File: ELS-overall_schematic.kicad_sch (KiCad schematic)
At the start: 3 parts, among them J1 DE9_Plug, J2 DE9_Plug, U1 LTC2851HDD

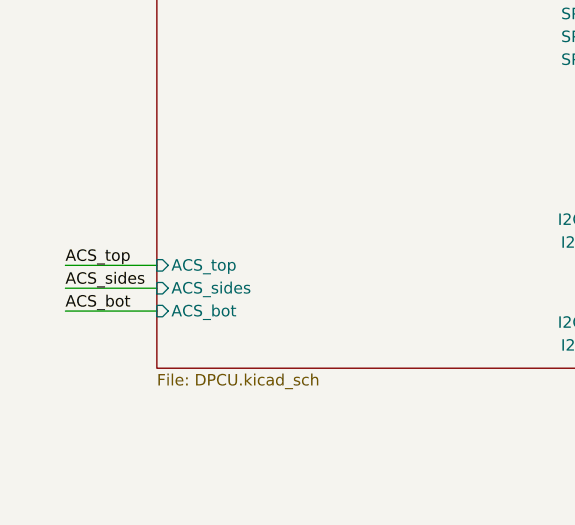
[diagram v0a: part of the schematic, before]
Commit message: Add voltage divider for adj signals
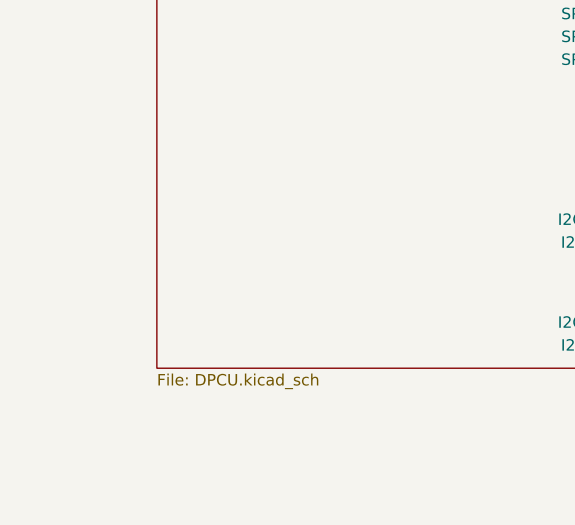
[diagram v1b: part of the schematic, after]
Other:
- sheet DPCU ports: added none; removed ACS_bot, ACS_sides, ACS_top
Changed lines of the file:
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@@
 	(wire
 		(pts
-			(xy 33.02 161.29) (xy 22.86 161.29)
-		)
-		(stroke
-			(width 0)
-			(type default)
-		)
-	)
-	(wire
-		(pts
 			(xy 153.67 77.47) (xy 163.83 77.47)
 		)
@@
 	(wire
 		(pts
-			(xy 33.02 163.83) (xy 22.86 163.83)
-		)
-		(stroke
-			(width 0)
-			(type default)
-		)
-	)
-	(wire
-		(pts
 			(xy 153.67 176.53) (xy 163.83 176.53)
 		)
@@
 	(wire
 		(pts
-			(xy 33.02 158.75) (xy 22.86 158.75)
-		)
-		(stroke
-			(width 0)
-			(type default)
-		)
-	)
-	(wire
-		(pts
 			(xy 203.2 118.11) (xy 195.58 118.11)
 		)
@@
 		)
 	)
-	(label "ACS_bot"
-		(at 22.86 163.83 0)
-		(fields_autoplaced yes)
-		(effects
-			(font
-				(size 1.27 1.27)
-			)
-			(justify left bottom)
-		)
-	)
 	(label "SDA2"
 		(at 203.2 83.82 180)
@@
 		)
 	)
-	(label "ACS_top"
-		(at 22.86 158.75 0)
-		(fields_autoplaced yes)
-		(effects
-			(font
-				(size 1.27 1.27)
-			)
-			(justify left bottom)
-		)
-	)
 	(label "SDA2"
 		(at 203.2 19.05 180)
@@
 		)
 	)
-	(label "ACS_sides"
-		(at 22.86 161.29 0)
-		(fields_autoplaced yes)
-		(effects
-			(font
-				(size 1.27 1.27)
-			)
-			(justify left bottom)
-		)
-	)
 	(label "ACS_bot"
 		(at 231.14 35.56 0)
@@
 			)
 		)
-		(pin "ACS_bot" input
-			(at 33.02 163.83 180)
-			(effects
-				(font
-					(size 1.27 1.27)
-				)
-				(justify left)
-			)
-		)
-		(pin "ACS_sides" input
-			(at 33.02 161.29 180)
-			(effects
-				(font
-					(size 1.27 1.27)
-				)
-				(justify left)
-			)
-		)
-		(pin "ACS_top" input
-			(at 33.02 158.75 180)
-			(effects
-				(font
-					(size 1.27 1.27)
-				)
-				(justify left)
-			)
-		)

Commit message: data ready signals
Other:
- sheet DAQ-A1 MCU ports: added DATA_READY; removed none
- sheet DAQ-A2 MCU ports: added DATA_READY; removed none
- sheet DAQ-B1 MCU ports: added DATA_READY; removed none
- sheet DAQ-B2 MCU ports: added DATA_READY; removed none
- sheet DPCU ports: added DATA_READY-A1, DATA_READY-A2, DATA_READY-B1, DATA_READY-B2, SPI1_CS-A1, SPI1_CS-A2, SPI1_CS-B1, SPI1_CS-B2; removed SPI1_CS1, SPI1_CS2, SPI1_CS3, SPI1_CS4
